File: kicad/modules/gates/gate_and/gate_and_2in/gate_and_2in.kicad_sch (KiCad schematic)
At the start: 2 parts, among them Q3901 PMOS, Q3902 NMOS

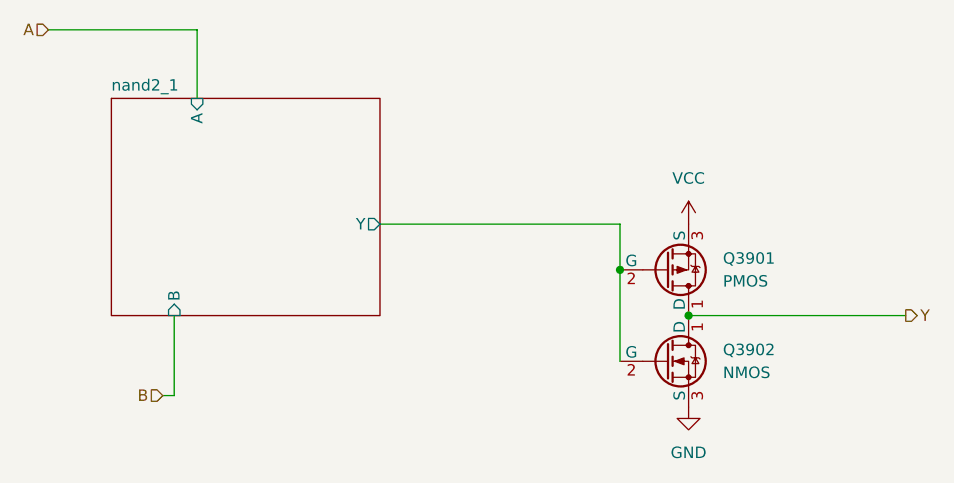
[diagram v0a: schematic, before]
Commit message: feat: complete circuit designs for all ALU components
* Designed all gate modules: AND, OR, NOT, NAND, NOR, XOR (1-bit and 8-bit variants)

* Completed multiplexer hierarchy: 2:1, 4:1, and 8:1 8-bit muxes

* Finalized add_sub board schematic and LED panel designs

* Added new board modules: flags, main_control, main_logic

* Updated Logisim top-level ALU circuit

* Note: KiCad directory path errors to be resolved next (iCloud sync issue), then begin PCB routing
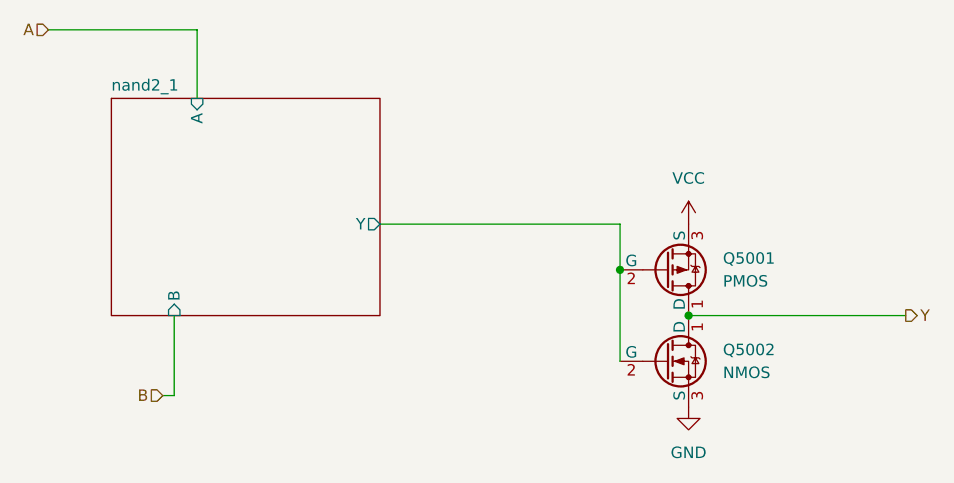
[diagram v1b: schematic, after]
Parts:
- renumbered Q3901 to Q5001, Q3902 to Q5002
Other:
- sheet nand2_1: file ../../modules/gates/gate_nand/gate_nand_2in/gate_nand_2in.kicad_sch -> ../../modules/gates/modules/gates/modules/gates/gate_nand/gate_nand_2in/gate_nand_2in.kicad_sch
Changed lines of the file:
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@@
 		(dnp no)
 		(fields_autoplaced yes)
-		(property "Reference" "#PWR03901"
+		(property "Reference" "#PWR?"
 			(at 129.54 53.34 0)
 			(effects
@@
 		(instances
 			(project "add_sub"
+				(path "/1a086df7-7508-4c0d-b696-2f052ea4c322/1ef1390d-554a-43ac-8488-88e316fc49f6"
+					(reference "#PWR05001")
+					(unit 1)
+				)
+				(path "/1a086df7-7508-4c0d-b696-2f052ea4c322/2f79ae65-f187-4eb0-b11c-b9a1e180c5dd"
+					(reference "#PWR03901")
+					(unit 1)
+				)
+				(path "/1a086df7-7508-4c0d-b696-2f052ea4c322/6ca409b3-ddc0-4229-85f3-d4326cd96ee4"
+					(reference "#PWR04701")
+					(unit 1)
+				)
 				(path "/1a086df7-7508-4c0d-b696-2f052ea4c322/92236a5d-2e44-4e21-b0a9-9f7c8d85dee0/072d980d-7920-4601-abce-27648096a13e/1b6dbcd7-da01-491e-a511-d4ca9e2e8ea4"
 					(reference "#PWR03901")
@@
 				(path "/1a086df7-7508-4c0d-b696-2f052ea4c322/92236a5d-2e44-4e21-b0a9-9f7c8d85dee0/e678a1db-fc7f-4871-8288-df3fa647bce0/7107c27b-a347-41a0-a389-70cfff67c775"
 					(reference "#PWR03201")
+					(unit 1)
+				)
+			)
+			(project "led_panel_3"
+				(path "/892e505f-6651-4aa4-9d30-6fa009555436/341c2c20-2781-43b7-8c5d-84ac7f9678c4"
+					(reference "#PWR?")
+					(unit 1)
+				)
+			)
+			(project "add_sub"
+				(path "/9c59990f-2fe5-4da7-bc07-d03b445b1465/5245a8e3-8b5a-48cc-b0e1-b80c6cdf1839"
+					(reference "#PWR05001")
+					(unit 1)
+				)
+			)
+			(project "add_sub"
+				(path "/e2bb65ff-e340-4712-a878-121a5433abf0/44dc33f2-40f3-4831-b606-5b0e04891a93"
+					(reference "#PWR05001")
 					(unit 1)
 				)
@@
 		(dnp no)
 		(fields_autoplaced yes)
-		(property "Reference" "Q3901"
+		(property "Reference" "Q?"
 			(at 133.35 53.3399 0)
 			(effects
@@
 		(instances
 			(project "add_sub"
+				(path "/1a086df7-7508-4c0d-b696-2f052ea4c322/1ef1390d-554a-43ac-8488-88e316fc49f6"
+					(reference "Q5001")
+					(unit 1)
+				)
+				(path "/1a086df7-7508-4c0d-b696-2f052ea4c322/2f79ae65-f187-4eb0-b11c-b9a1e180c5dd"
+					(reference "Q3901")
+					(unit 1)
+				)
+				(path "/1a086df7-7508-4c0d-b696-2f052ea4c322/6ca409b3-ddc0-4229-85f3-d4326cd96ee4"
+					(reference "Q4701")
+					(unit 1)
+				)
 				(path "/1a086df7-7508-4c0d-b696-2f052ea4c322/92236a5d-2e44-4e21-b0a9-9f7c8d85dee0/072d980d-7920-4601-abce-27648096a13e/1b6dbcd7-da01-491e-a511-d4ca9e2e8ea4"
 					(reference "Q3901")
@@
 				(path "/1a086df7-7508-4c0d-b696-2f052ea4c322/92236a5d-2e44-4e21-b0a9-9f7c8d85dee0/e678a1db-fc7f-4871-8288-df3fa647bce0/7107c27b-a347-41a0-a389-70cfff67c775"
 					(reference "Q3201")
+					(unit 1)
+				)
+			)
+			(project "led_panel_3"
+				(path "/892e505f-6651-4aa4-9d30-6fa009555436/341c2c20-2781-43b7-8c5d-84ac7f9678c4"
+					(reference "Q?")
+					(unit 1)
+				)
+			)
+			(project "add_sub"
+				(path "/9c59990f-2fe5-4da7-bc07-d03b445b1465/5245a8e3-8b5a-48cc-b0e1-b80c6cdf1839"
+					(reference "Q5001")
+					(unit 1)
+				)
+			)
+			(project "add_sub"
+				(path "/e2bb65ff-e340-4712-a878-121a5433abf0/44dc33f2-40f3-4831-b606-5b0e04891a93"
+					(reference "Q5001")
 					(unit 1)
 				)
@@
 		(dnp no)
 		(fields_autoplaced yes)
-		(property "Reference" "Q3902"
+		(property "Reference" "Q?"
 			(at 133.35 63.4999 0)
 			(effects
@@
 		(instances
 			(project "add_sub"
+				(path "/1a086df7-7508-4c0d-b696-2f052ea4c322/1ef1390d-554a-43ac-8488-88e316fc49f6"
+					(reference "Q5002")
+					(unit 1)
+				)
+				(path "/1a086df7-7508-4c0d-b696-2f052ea4c322/2f79ae65-f187-4eb0-b11c-b9a1e180c5dd"
+					(reference "Q3902")
+					(unit 1)
+				)
+				(path "/1a086df7-7508-4c0d-b696-2f052ea4c322/6ca409b3-ddc0-4229-85f3-d4326cd96ee4"
+					(reference "Q4702")
+					(unit 1)
+				)
 				(path "/1a086df7-7508-4c0d-b696-2f052ea4c322/92236a5d-2e44-4e21-b0a9-9f7c8d85dee0/072d980d-7920-4601-abce-27648096a13e/1b6dbcd7-da01-491e-a511-d4ca9e2e8ea4"
 					(reference "Q3902")
@@
 				(path "/1a086df7-7508-4c0d-b696-2f052ea4c322/92236a5d-2e44-4e21-b0a9-9f7c8d85dee0/e678a1db-fc7f-4871-8288-df3fa647bce0/7107c27b-a347-41a0-a389-70cfff67c775"
 					(reference "Q3202")
+					(unit 1)
+				)
+			)
+			(project "led_panel_3"
+				(path "/892e505f-6651-4aa4-9d30-6fa009555436/341c2c20-2781-43b7-8c5d-84ac7f9678c4"
+					(reference "Q?")
+					(unit 1)
+				)
+			)
+			(project "add_sub"
+				(path "/9c59990f-2fe5-4da7-bc07-d03b445b1465/5245a8e3-8b5a-48cc-b0e1-b80c6cdf1839"
+					(reference "Q5002")
+					(unit 1)
+				)
+			)
+			(project "add_sub"
+				(path "/e2bb65ff-e340-4712-a878-121a5433abf0/44dc33f2-40f3-4831-b606-5b0e04891a93"
+					(reference "Q5002")
 					(unit 1)
 				)
@@
 		(dnp no)
 		(fields_autoplaced yes)
-		(property "Reference" "#PWR03902"
+		(property "Reference" "#PWR?"
 			(at 129.54 76.2 0)
 			(effects
@@
 		(instances
 			(project "add_sub"
+				(path "/1a086df7-7508-4c0d-b696-2f052ea4c322/1ef1390d-554a-43ac-8488-88e316fc49f6"
+					(reference "#PWR05002")
+					(unit 1)
+				)
+				(path "/1a086df7-7508-4c0d-b696-2f052ea4c322/2f79ae65-f187-4eb0-b11c-b9a1e180c5dd"
+					(reference "#PWR03902")
+					(unit 1)
+				)
+				(path "/1a086df7-7508-4c0d-b696-2f052ea4c322/6ca409b3-ddc0-4229-85f3-d4326cd96ee4"
+					(reference "#PWR04702")
+					(unit 1)
+				)
 				(path "/1a086df7-7508-4c0d-b696-2f052ea4c322/92236a5d-2e44-4e21-b0a9-9f7c8d85dee0/072d980d-7920-4601-abce-27648096a13e/1b6dbcd7-da01-491e-a511-d4ca9e2e8ea4"
 					(reference "#PWR03902")
@@
 				(path "/1a086df7-7508-4c0d-b696-2f052ea4c322/92236a5d-2e44-4e21-b0a9-9f7c8d85dee0/e678a1db-fc7f-4871-8288-df3fa647bce0/7107c27b-a347-41a0-a389-70cfff67c775"
 					(reference "#PWR03202")
+					(unit 1)
+				)
+			)
+			(project "led_panel_3"
+				(path "/892e505f-6651-4aa4-9d30-6fa009555436/341c2c20-2781-43b7-8c5d-84ac7f9678c4"
+					(reference "#PWR?")
+					(unit 1)
+				)
+			)
+			(project "add_sub"
+				(path "/9c59990f-2fe5-4da7-bc07-d03b445b1465/5245a8e3-8b5a-48cc-b0e1-b80c6cdf1839"
+					(reference "#PWR05002")
+					(unit 1)
+				)
+			)
+			(project "add_sub"
+				(path "/e2bb65ff-e340-4712-a878-121a5433abf0/44dc33f2-40f3-4831-b606-5b0e04891a93"
+					(reference "#PWR05002")
 					(unit 1)
 				)
@@
 			)
 		)
-		(property "Sheetfile" "../../modules/gates/gate_nand/gate_nand_2in/gate_nand_2in.kicad_sch"
+		(property "Sheetfile" "../../modules/gates/modules/gates/modules/gates/gate_nand/gate_nand_2in/gate_nand_2in.kicad_sch"
 			(at 65.405 60.2746 0)
 			(effects
@@
 					(page "45")
 				)
-			)
+				(path "/1a086df7-7508-4c0d-b696-2f052ea4c322/2f79ae65-f187-4eb0-b11c-b9a1e180c5dd"
+					(page "46")
+				)
+				(path "/1a086df7-7508-4c0d-b696-2f052ea4c322/6ca409b3-ddc0-4229-85f3-d4326cd96ee4"
+					(page "48")
+				)
+				(path "/1a086df7-7508-4c0d-b696-2f052ea4c322/1ef1390d-554a-43ac-8488-88e316fc49f6"
+					(page "53")
+				)
+			)
+			(project ""
+				(path "/5245a8e3-8b5a-48cc-b0e1-b80c6cdf1839"
+					(page "#")
+				)
+			)
+			(project "main_logic"
+				(path "/9c59990f-2fe5-4da7-bc07-d03b445b1465/5245a8e3-8b5a-48cc-b0e1-b80c6cdf1839"
+					(page "32")
+				)
+			)
+			(project ""
+				(path "/44dc33f2-40f3-4831-b606-5b0e04891a93"
+					(page "#")
+				)
+			)
+			(project "main_control"
+				(path "/e2bb65ff-e340-4712-a878-121a5433abf0/44dc33f2-40f3-4831-b606-5b0e04891a93"
+					(page "7")
+				)
+			)

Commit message: Fix KiCad file paths and complete core circuit design
- Fixed file path errors across all KiCad schematics and projects
- Completed core circuit designs:
  * Adder and subtractor modules (adder2, adder8)
  * LED panels (led_panel_1) with display circuits
  * Flag LED circuits for status indicators
  * All dependent logic gate modules (AND, OR, NOT, NAND, NOR, XOR)
  * All multiplexer modules (2:1, 4:1, 8:1, 8-bit)
  * Main control board schematics
  * Flags board schematics
- Updated .gitignore to exclude KiCad backups, cache files, and lock files
- Ready for pin placement and routing of control buses, power rails, and inter-board signals
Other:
- sheet nand2_1: file ../../modules/gates/modules/gates/modules/gates/gate_nand/gate_nand_2in/gate_nand_2in.kicad_sch -> ../../gate_nand/gate_nand_2in/gate_nand_2in.kicad_sch
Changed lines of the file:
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@@
 				)
 				(path "/1a086df7-7508-4c0d-b696-2f052ea4c322/2f79ae65-f187-4eb0-b11c-b9a1e180c5dd"
-					(reference "#PWR03901")
+					(reference "#PWR05201")
 					(unit 1)
 				)
@@
 				)
 				(path "/1a086df7-7508-4c0d-b696-2f052ea4c322/92236a5d-2e44-4e21-b0a9-9f7c8d85dee0/0a1186b3-be7e-452c-80fb-048fb270c396/1b6dbcd7-da01-491e-a511-d4ca9e2e8ea4"
-					(reference "#PWR03901")
+					(reference "#PWR01701")
 					(unit 1)
 				)
@@
 				)
 				(path "/1a086df7-7508-4c0d-b696-2f052ea4c322/92236a5d-2e44-4e21-b0a9-9f7c8d85dee0/5ca3f5ef-5ebe-454d-ad68-04b74d36a9c7/1b6dbcd7-da01-491e-a511-d4ca9e2e8ea4"
-					(reference "#PWR03901")
+					(reference "#PWR0303")
 					(unit 1)
 				)
@@
 				)
 			)
+			(project "gate_and_2in"
+				(path "/68c84310-9fae-4691-b1f0-f5a25f3b9dcf"
+					(reference "#PWR?")
+					(unit 1)
+				)
+			)
 			(project "led_panel_3"
 				(path "/892e505f-6651-4aa4-9d30-6fa009555436/341c2c20-2781-43b7-8c5d-84ac7f9678c4"
@@
 				)
 			)
-			(project "add_sub"
-				(path "/9c59990f-2fe5-4da7-bc07-d03b445b1465/5245a8e3-8b5a-48cc-b0e1-b80c6cdf1839"
-					(reference "#PWR05001")
-					(unit 1)
-				)
-			)
-			(project "add_sub"
-				(path "/e2bb65ff-e340-4712-a878-121a5433abf0/44dc33f2-40f3-4831-b606-5b0e04891a93"
-					(reference "#PWR05001")
+			(project "adder2"
+				(path "/e938a6bb-35cc-48f7-b2cb-f9f5c6ada261/1b6dbcd7-da01-491e-a511-d4ca9e2e8ea4"
+					(reference "#PWR?")
+					(unit 1)
+				)
+				(path "/e938a6bb-35cc-48f7-b2cb-f9f5c6ada261/397a65b0-fa09-46e2-a635-83b6e803a27d"
+					(reference "#PWR?")
+					(unit 1)
+				)
+				(path "/e938a6bb-35cc-48f7-b2cb-f9f5c6ada261/41319973-b7d8-4970-b6d6-1b592f5caee3"
+					(reference "#PWR?")
+					(unit 1)
+				)
+				(path "/e938a6bb-35cc-48f7-b2cb-f9f5c6ada261/7107c27b-a347-41a0-a389-70cfff67c775"
+					(reference "#PWR?")
 					(unit 1)
 				)
@@
 				)
 				(path "/1a086df7-7508-4c0d-b696-2f052ea4c322/2f79ae65-f187-4eb0-b11c-b9a1e180c5dd"
-					(reference "Q3901")
+					(reference "Q5201")
 					(unit 1)
 				)
@@
 				)
 				(path "/1a086df7-7508-4c0d-b696-2f052ea4c322/92236a5d-2e44-4e21-b0a9-9f7c8d85dee0/0a1186b3-be7e-452c-80fb-048fb270c396/1b6dbcd7-da01-491e-a511-d4ca9e2e8ea4"
-					(reference "Q3901")
+					(reference "Q1701")
 					(unit 1)
 				)
@@
 				)
 				(path "/1a086df7-7508-4c0d-b696-2f052ea4c322/92236a5d-2e44-4e21-b0a9-9f7c8d85dee0/5ca3f5ef-5ebe-454d-ad68-04b74d36a9c7/1b6dbcd7-da01-491e-a511-d4ca9e2e8ea4"
-					(reference "Q3901")
+					(reference "Q305")
 					(unit 1)
 				)
@@
 				)
 			)
+			(project "gate_and_2in"
+				(path "/68c84310-9fae-4691-b1f0-f5a25f3b9dcf"
+					(reference "Q?")
+					(unit 1)
+				)
+			)
 			(project "led_panel_3"
 				(path "/892e505f-6651-4aa4-9d30-6fa009555436/341c2c20-2781-43b7-8c5d-84ac7f9678c4"
@@
 				)
 			)
-			(project "add_sub"
-				(path "/9c59990f-2fe5-4da7-bc07-d03b445b1465/5245a8e3-8b5a-48cc-b0e1-b80c6cdf1839"
-					(reference "Q5001")
-					(unit 1)
-				)
-			)
-			(project "add_sub"
-				(path "/e2bb65ff-e340-4712-a878-121a5433abf0/44dc33f2-40f3-4831-b606-5b0e04891a93"
-					(reference "Q5001")
+			(project "adder2"
+				(path "/e938a6bb-35cc-48f7-b2cb-f9f5c6ada261/1b6dbcd7-da01-491e-a511-d4ca9e2e8ea4"
+					(reference "Q?")
+					(unit 1)
+				)
+				(path "/e938a6bb-35cc-48f7-b2cb-f9f5c6ada261/397a65b0-fa09-46e2-a635-83b6e803a27d"
+					(reference "Q?")
+					(unit 1)
+				)
+				(path "/e938a6bb-35cc-48f7-b2cb-f9f5c6ada261/41319973-b7d8-4970-b6d6-1b592f5caee3"
+					(reference "Q?")
+					(unit 1)
+				)
+				(path "/e938a6bb-35cc-48f7-b2cb-f9f5c6ada261/7107c27b-a347-41a0-a389-70cfff67c775"
+					(reference "Q?")
 					(unit 1)
 				)
@@
 				)
 				(path "/1a086df7-7508-4c0d-b696-2f052ea4c322/2f79ae65-f187-4eb0-b11c-b9a1e180c5dd"
-					(reference "Q3902")
+					(reference "Q5202")
 					(unit 1)
 				)
@@
 				)
 				(path "/1a086df7-7508-4c0d-b696-2f052ea4c322/92236a5d-2e44-4e21-b0a9-9f7c8d85dee0/0a1186b3-be7e-452c-80fb-048fb270c396/1b6dbcd7-da01-491e-a511-d4ca9e2e8ea4"
-					(reference "Q3902")
+					(reference "Q1702")
 					(unit 1)
 				)
@@
 				)
 				(path "/1a086df7-7508-4c0d-b696-2f052ea4c322/92236a5d-2e44-4e21-b0a9-9f7c8d85dee0/5ca3f5ef-5ebe-454d-ad68-04b74d36a9c7/1b6dbcd7-da01-491e-a511-d4ca9e2e8ea4"
-					(reference "Q3902")
+					(reference "Q306")
 					(unit 1)
 				)
@@
 				)
 			)
+			(project "gate_and_2in"
+				(path "/68c84310-9fae-4691-b1f0-f5a25f3b9dcf"
+					(reference "Q?")
+					(unit 1)
+				)
+			)
 			(project "led_panel_3"
 				(path "/892e505f-6651-4aa4-9d30-6fa009555436/341c2c20-2781-43b7-8c5d-84ac7f9678c4"
@@
 				)
 			)
-			(project "add_sub"
-				(path "/9c59990f-2fe5-4da7-bc07-d03b445b1465/5245a8e3-8b5a-48cc-b0e1-b80c6cdf1839"
-					(reference "Q5002")
-					(unit 1)
-				)
-			)
-			(project "add_sub"
-				(path "/e2bb65ff-e340-4712-a878-121a5433abf0/44dc33f2-40f3-4831-b606-5b0e04891a93"
-					(reference "Q5002")
+			(project "adder2"
+				(path "/e938a6bb-35cc-48f7-b2cb-f9f5c6ada261/1b6dbcd7-da01-491e-a511-d4ca9e2e8ea4"
+					(reference "Q?")
+					(unit 1)
+				)
+				(path "/e938a6bb-35cc-48f7-b2cb-f9f5c6ada261/397a65b0-fa09-46e2-a635-83b6e803a27d"
+					(reference "Q?")
+					(unit 1)
+				)
+				(path "/e938a6bb-35cc-48f7-b2cb-f9f5c6ada261/41319973-b7d8-4970-b6d6-1b592f5caee3"
+					(reference "Q?")
+					(unit 1)
+				)
+				(path "/e938a6bb-35cc-48f7-b2cb-f9f5c6ada261/7107c27b-a347-41a0-a389-70cfff67c775"
+					(reference "Q?")
 					(unit 1)
 				)
@@
 				)
 				(path "/1a086df7-7508-4c0d-b696-2f052ea4c322/2f79ae65-f187-4eb0-b11c-b9a1e180c5dd"
-					(reference "#PWR03902")
+					(reference "#PWR05202")
 					(unit 1)
 				)
@@
 				)
 				(path "/1a086df7-7508-4c0d-b696-2f052ea4c322/92236a5d-2e44-4e21-b0a9-9f7c8d85dee0/0a1186b3-be7e-452c-80fb-048fb270c396/1b6dbcd7-da01-491e-a511-d4ca9e2e8ea4"
-					(reference "#PWR03902")
+					(reference "#PWR01702")
 					(unit 1)
 				)
@@
 				)
 				(path "/1a086df7-7508-4c0d-b696-2f052ea4c322/92236a5d-2e44-4e21-b0a9-9f7c8d85dee0/5ca3f5ef-5ebe-454d-ad68-04b74d36a9c7/1b6dbcd7-da01-491e-a511-d4ca9e2e8ea4"
-					(reference "#PWR03902")
+					(reference "#PWR0304")
 					(unit 1)
 				)
@@
 				)
 			)
+			(project "gate_and_2in"
+				(path "/68c84310-9fae-4691-b1f0-f5a25f3b9dcf"
+					(reference "#PWR?")
+					(unit 1)
+				)
+			)
 			(project "led_panel_3"
 				(path "/892e505f-6651-4aa4-9d30-6fa009555436/341c2c20-2781-43b7-8c5d-84ac7f9678c4"
@@
 				)
 			)
-			(project "add_sub"
-				(path "/9c59990f-2fe5-4da7-bc07-d03b445b1465/5245a8e3-8b5a-48cc-b0e1-b80c6cdf1839"
-					(reference "#PWR05002")
-					(unit 1)
-				)
-			)
-			(project "add_sub"
-				(path "/e2bb65ff-e340-4712-a878-121a5433abf0/44dc33f2-40f3-4831-b606-5b0e04891a93"
-					(reference "#PWR05002")
+			(project "adder2"
+				(path "/e938a6bb-35cc-48f7-b2cb-f9f5c6ada261/1b6dbcd7-da01-491e-a511-d4ca9e2e8ea4"
+					(reference "#PWR?")
+					(unit 1)
+				)
+				(path "/e938a6bb-35cc-48f7-b2cb-f9f5c6ada261/397a65b0-fa09-46e2-a635-83b6e803a27d"
+					(reference "#PWR?")
+					(unit 1)
+				)
+				(path "/e938a6bb-35cc-48f7-b2cb-f9f5c6ada261/41319973-b7d8-4970-b6d6-1b592f5caee3"
+					(reference "#PWR?")
+					(unit 1)
+				)
+				(path "/e938a6bb-35cc-48f7-b2cb-f9f5c6ada261/7107c27b-a347-41a0-a389-70cfff67c775"
+					(reference "#PWR?")
 					(unit 1)
 				)
@@
 			)
 		)
-		(property "Sheetfile" "../../modules/gates/modules/gates/modules/gates/gate_nand/gate_nand_2in/gate_nand_2in.kicad_sch"
+		(property "Sheetfile" "../../gate_nand/gate_nand_2in/gate_nand_2in.kicad_sch"
 			(at 65.405 60.2746 0)
 			(effects
@@
 				)
 			)
+			(project "gate_and_2in"
+				(path "/68c84310-9fae-4691-b1f0-f5a25f3b9dcf"
+					(page "2")
+				)
+			)
+			(project "adder2"
+				(path "/e938a6bb-35cc-48f7-b2cb-f9f5c6ada261/1b6dbcd7-da01-491e-a511-d4ca9e2e8ea4"
+					(page "3")
+				)
+				(path "/e938a6bb-35cc-48f7-b2cb-f9f5c6ada261/41319973-b7d8-4970-b6d6-1b592f5caee3"
+					(page "5")
+				)
+				(path "/e938a6bb-35cc-48f7-b2cb-f9f5c6ada261/7107c27b-a347-41a0-a389-70cfff67c775"
+					(page "7")
+				)
+				(path "/e938a6bb-35cc-48f7-b2cb-f9f5c6ada261/397a65b0-fa09-46e2-a635-83b6e803a27d"
+					(page "9")
+				)
+			)
 		)
 	)
+	(sheet_instances
+		(path "/"
+			(page "1")
+		)
+	)
+	(embedded_fonts no)
 )
